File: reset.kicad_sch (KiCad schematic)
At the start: 21 parts, among them J4 MAINCLK

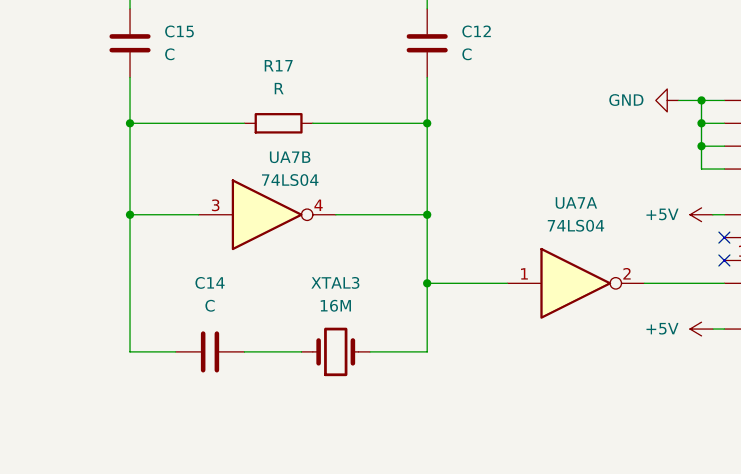
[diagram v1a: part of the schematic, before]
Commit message: Annotated all components
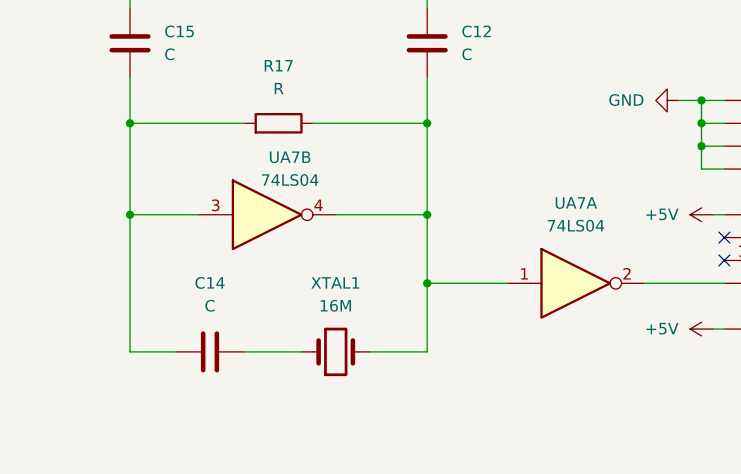
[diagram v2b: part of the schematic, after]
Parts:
- renumbered XTAL3 to XTAL1
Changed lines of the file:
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@@
 		(dnp no)
 		(fields_autoplaced yes)
-		(property "Reference" "XTAL3"
+		(property "Reference" "XTAL1"
 			(at 43.18 177.8 0)
 			(effects
@@
 			(project "ceda"
 				(path "/12a6dbe3-008d-4c5b-88f6-9f1c816060be/d9e42cc5-3ed8-41e5-aab1-e3ef5c13a809"
-					(reference "XTAL3")
+					(reference "XTAL1")
 					(unit 1)
 				)

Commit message: Assigned default footprints to ICs
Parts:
- UA6, UH16: footprint (none) -> Package_DIP:DIP-16_W7.62mm
- UA7, UD14, UD3, UF16, UH15, UL7: footprint (none) -> Package_DIP:DIP-14_W7.62mm
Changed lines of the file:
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@@
 			)
 		)
-		(property "Footprint" ""
+		(property "Footprint" "Package_DIP:DIP-14_W7.62mm"
 			(at 137.16 97.79 0)
 			(effects
@@
 			)
 		)
-		(property "Footprint" ""
+		(property "Footprint" "Package_DIP:DIP-16_W7.62mm"
 			(at 99.06 170.18 0)
 			(effects
@@
 			)
 		)
-		(property "Footprint" ""
+		(property "Footprint" "Package_DIP:DIP-14_W7.62mm"
 			(at 53.34 45.72 0)
 			(effects
@@
 			)
 		)
-		(property "Footprint" ""
+		(property "Footprint" "Package_DIP:DIP-14_W7.62mm"
 			(at 146.05 161.29 0)
 			(effects
@@
 			)
 		)
-		(property "Footprint" ""
+		(property "Footprint" "Package_DIP:DIP-14_W7.62mm"
 			(at 222.25 87.63 0)
 			(effects
@@
 			)
 		)
-		(property "Footprint" ""
+		(property "Footprint" "Package_DIP:DIP-14_W7.62mm"
 			(at 185.42 72.39 0)
 			(effects
@@
 			)
 		)
-		(property "Footprint" ""
+		(property "Footprint" "Package_DIP:DIP-14_W7.62mm"
 			(at 204.47 72.39 0)
 			(effects
@@
 			)
 		)
-		(property "Footprint" ""
+		(property "Footprint" "Package_DIP:DIP-16_W7.62mm"
 			(at 132.08 59.69 0)
 			(effects
@@
 			)
 		)
-		(property "Footprint" ""
+		(property "Footprint" "Package_DIP:DIP-14_W7.62mm"
 			(at 66.04 72.39 0)
 			(effects
@@
 			)
 		)
-		(property "Footprint" ""
+		(property "Footprint" "Package_DIP:DIP-14_W7.62mm"
 			(at 146.05 181.61 0)
 			(effects
@@
 			)
 		)
-		(property "Footprint" ""
+		(property "Footprint" "Package_DIP:DIP-14_W7.62mm"
 			(at 35.56 170.18 0)
 			(effects
@@
 			)
 		)
-		(property "Footprint" ""
+		(property "Footprint" "Package_DIP:DIP-14_W7.62mm"
 			(at 146.05 171.45 0)
 			(effects
@@
 			)
 		)
-		(property "Footprint" ""
+		(property "Footprint" "Package_DIP:DIP-14_W7.62mm"
 			(at 69.85 177.8 0)
 			(effects
@@
 			)
 		)
-		(property "Footprint" ""
+		(property "Footprint" "Package_DIP:DIP-14_W7.62mm"
 			(at 86.36 59.69 0)
 			(effects

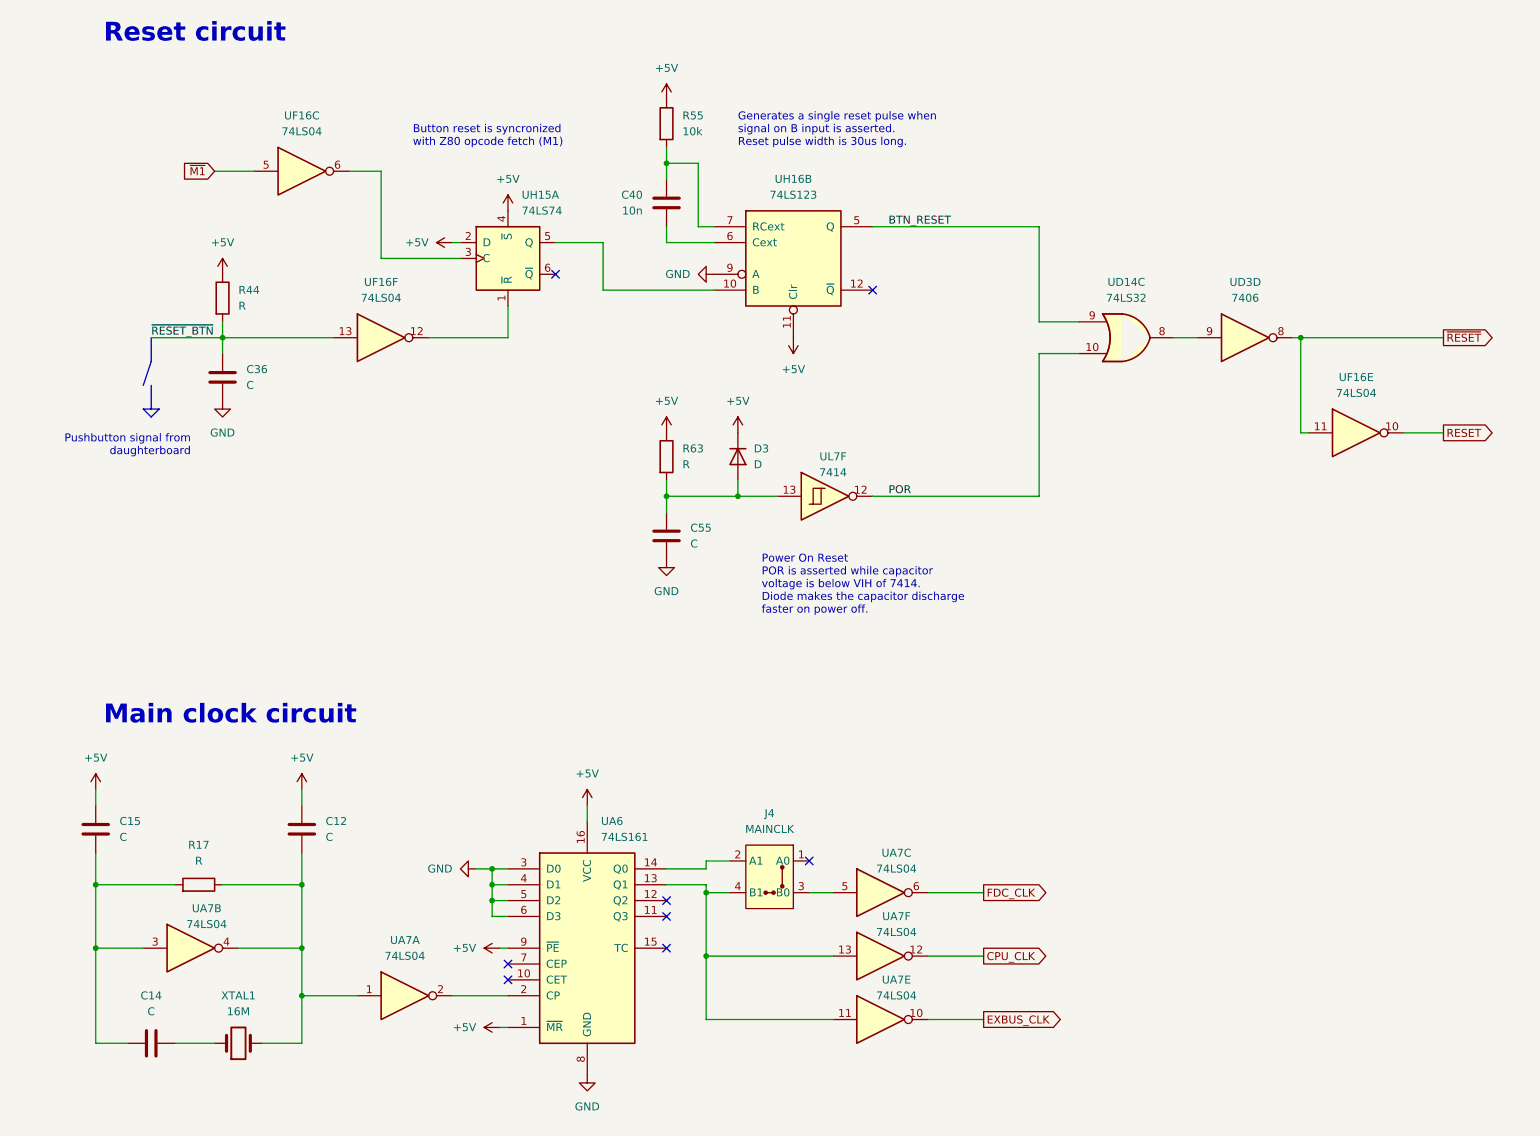
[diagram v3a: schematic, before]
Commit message: pcb: added and placed almost all components
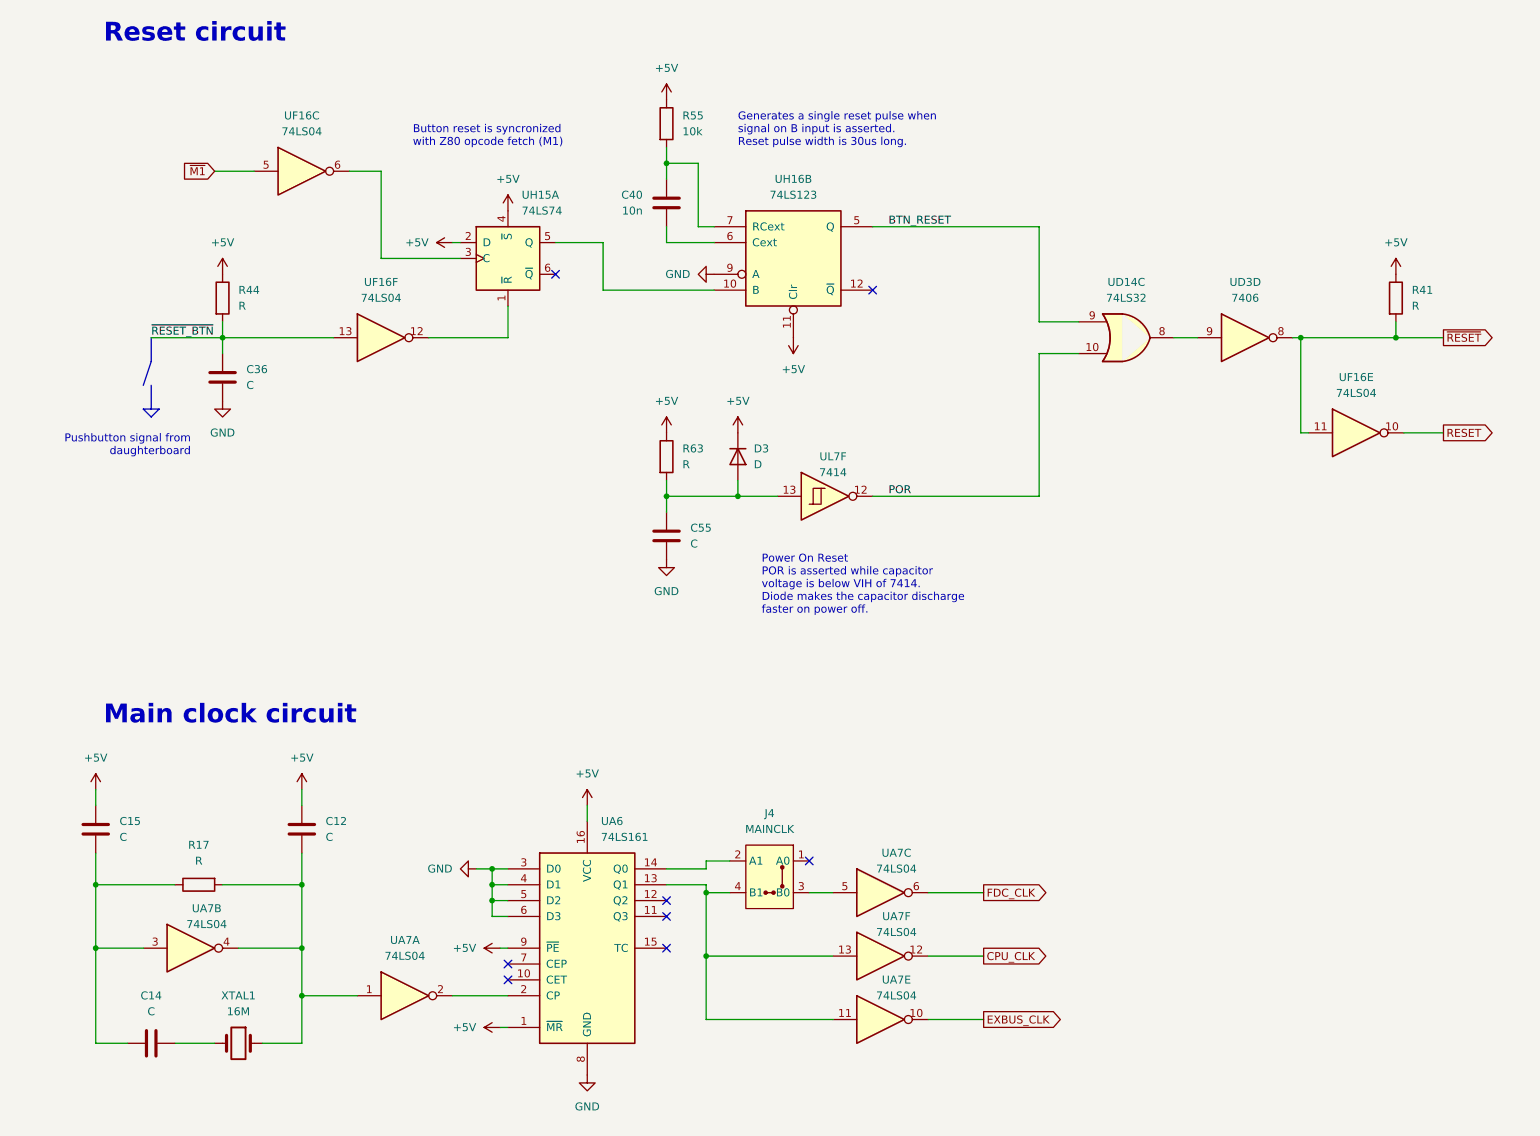
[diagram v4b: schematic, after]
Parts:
- added R41: R, Resistor_THT:R_Axial_DIN0204_L3.6mm_D1.6mm_P5.08mm_Vertical, symbol Device:R
- C12, C14, C15, C36, C40, C55: footprint (none) -> Capacitor_THT:C_Disc_D4.3mm_W1.9mm_P5.00mm
- D3: footprint (none) -> Diode_THT:D_A-405_P5.08mm_Vertical_KathodeUp
- J4: footprint (none) -> Connector_PinHeader_2.54mm:PinHeader_2x02_P2.54mm_Vertical
- R17, R44, R63: footprint (none) -> Resistor_THT:R_Axial_DIN0204_L3.6mm_D1.6mm_P5.08mm_Vertical
- R55: footprint (none) -> Resistor_THT:R_Axial_DIN0309_L9.0mm_D3.2mm_P12.70mm_Horizontal
- XTAL1: footprint (none) -> Crystal:Crystal_HC18-U_Vertical
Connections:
- net +5V: now also R41.1
- net ~{RESET}: now also R41.2
- net at C14.2, C15.1, UA7.3: now also R17.1; no longer R17.2
- net at C14.1: now also XTAL1.2; no longer XTAL1.1
- net at C12.1, UA7.1, UA7.4: now also R17.2, XTAL1.1; no longer R17.1, XTAL1.2
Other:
- moved on the sheet: R17
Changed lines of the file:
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@@
 	)
 	(junction
+		(at 228.6 72.39)
+		(diameter 0)
+		(color 0 0 0 0)
+	)
+	(junction
 		(at 20.32 160.02)
 		(diameter 0)
@@
 	(wire
 		(pts
-			(xy 213.36 72.39) (xy 236.22 72.39)
+			(xy 213.36 72.39) (xy 228.6 72.39)
 		)
 		(stroke
@@
 	(wire
 		(pts
+			(xy 228.6 69.85) (xy 228.6 72.39)
+		)
+		(stroke
+			(width 0)
+			(type default)
+		)
+	)
+	(wire
+		(pts
 			(xy 78.74 57.15) (xy 77.47 57.15)
 		)
@@
 	(wire
 		(pts
+			(xy 228.6 72.39) (xy 236.22 72.39)
+		)
+		(stroke
+			(width 0)
+			(type default)
+		)
+	)
+	(wire
+		(pts
 			(xy 85.09 170.18) (xy 86.36 170.18)
 		)
@@
 	)
 	(symbol
+		(lib_id "Device:R")
+		(at 228.6 66.04 0)
+		(unit 1)
+		(exclude_from_sim no)
+		(in_bom yes)
+		(on_board yes)
+		(dnp no)
+		(fields_autoplaced yes)
+		(property "Reference" "R41"
+			(at 231.14 64.7699 0)
+			(effects
+				(font
+					(size 1.27 1.27)
+				)
+				(justify left)
+			)
+		)
+		(property "Value" "R"
+			(at 231.14 67.3099 0)
+			(effects
+				(font
+					(size 1.27 1.27)
+				)
+				(justify left)
+			)
+		)
+		(property "Footprint" "Resistor_THT:R_Axial_DIN0204_L3.6mm_D1.6mm_P5.08mm_Vertical"
+			(at 226.822 66.04 90)
+			(effects
+				(font
+					(size 1.27 1.27)
+				)
+				(hide yes)
+			)
+		)
+		(property "Datasheet" "~"
+			(at 228.6 66.04 0)
+			(effects
+				(font
+					(size 1.27 1.27)
+				)
+				(hide yes)
+			)
+		)
+		(property "Description" ""
+			(at 228.6 66.04 0)
+			(effects
+				(font
+					(size 1.27 1.27)
+				)
+			)
+		)
+		(pin "1"
+		)
+		(pin "2"
+		)
+		(instances
+			(project "ceda"
+				(path "/12a6dbe3-008d-4c5b-88f6-9f1c816060be/d9e42cc5-3ed8-41e5-aab1-e3ef5c13a809"
+					(reference "R41")
+					(unit 1)
+				)
+			)
+		)
+	)
+	(symbol
 		(lib_id "74xx:74LS14")
 		(at 137.16 97.79 0)
@@
 			)
 		)
-		(property "Footprint" ""
+		(property "Footprint" "Capacitor_THT:C_Disc_D4.3mm_W1.9mm_P5.00mm"
 			(at 19.3548 147.32 0)
 			(effects
@@
 	)
 	(symbol
+		(lib_id "power:+5V")
+		(at 228.6 62.23 0)
+		(unit 1)
+		(exclude_from_sim no)
+		(in_bom yes)
+		(on_board yes)
+		(dnp no)
+		(fields_autoplaced yes)
+		(property "Reference" "#PWR03"
+			(at 228.6 66.04 0)
+			(effects
+				(font
+					(size 1.27 1.27)
+				)
+				(hide yes)
+			)
+		)
+		(property "Value" "+5V"
+			(at 228.6 57.15 0)
+			(effects
+				(font
+					(size 1.27 1.27)
+				)
+			)
+		)
+		(property "Footprint" ""
+			(at 228.6 62.23 0)
+			(effects
+				(font
+					(size 1.27 1.27)
+				)
+				(hide yes)
+			)
+		)
+		(property "Datasheet" ""
+			(at 228.6 62.23 0)
+			(effects
+				(font
+					(size 1.27 1.27)
+				)
+				(hide yes)
+			)
+		)
+		(property "Description" ""
+			(at 228.6 62.23 0)
+			(effects
+				(font
+					(size 1.27 1.27)
+				)
+			)
+		)
+		(pin "1"
+		)
+		(instances
+			(project "ceda"
+				(path "/12a6dbe3-008d-4c5b-88f6-9f1c816060be/d9e42cc5-3ed8-41e5-aab1-e3ef5c13a809"
+					(reference "#PWR03")
+					(unit 1)
+				)
+			)
+		)
+	)
+	(symbol
 		(lib_id "74xx:74LS04")
 		(at 222.25 87.63 0)
@@
 			)
 		)
-		(property "Footprint" ""
+		(property "Footprint" "Resistor_THT:R_Axial_DIN0204_L3.6mm_D1.6mm_P5.08mm_Vertical"
 			(at 109.982 91.44 90)
 			(effects
@@
 			)
 		)
-		(property "Footprint" ""
+		(property "Footprint" "Capacitor_THT:C_Disc_D4.3mm_W1.9mm_P5.00mm"
 			(at 25.4 184.4548 0)
 			(effects
@@
 			)
 		)
-		(property "Footprint" ""
+		(property "Footprint" "Diode_THT:D_A-405_P5.08mm_Vertical_KathodeUp"
 			(at 123.19 91.44 0)
 			(effects
@@
 			)
 		)
-		(property "Footprint" ""
+		(property "Footprint" "Capacitor_THT:C_Disc_D4.3mm_W1.9mm_P5.00mm"
 			(at 112.7252 54.61 0)
 			(effects
@@
 			)
 		)
-		(property "Footprint" ""
+		(property "Footprint" "Capacitor_THT:C_Disc_D4.3mm_W1.9mm_P5.00mm"
 			(at 112.7252 107.95 0)
 			(effects
@@
 			)
 		)
-		(property "Footprint" ""
+		(property "Footprint" "Resistor_THT:R_Axial_DIN0309_L9.0mm_D3.2mm_P12.70mm_Horizontal"
 			(at 109.982 38.1 90)
 			(effects
@@
 			)
 		)
-		(property "Footprint" ""
+		(property "Footprint" "Capacitor_THT:C_Disc_D4.3mm_W1.9mm_P5.00mm"
 			(at 52.3748 147.32 0)
 			(effects
@@
 	(symbol
 		(lib_id "Device:R")
-		(at 36.83 160.02 270)
+		(at 36.83 160.02 90)
 		(mirror x)
 		(unit 1)
@@
 			)
 		)
-		(property "Footprint" ""
-			(at 36.83 161.798 90)
+		(property "Footprint" "Resistor_THT:R_Axial_DIN0204_L3.6mm_D1.6mm_P5.08mm_Vertical"
+			(at 36.83 158.242 90)
 			(effects
 				(font
@@
 			)
 		)
-		(property "Footprint" ""
+		(property "Footprint" "Connector_PinHeader_2.54mm:PinHeader_2x02_P2.54mm_Vertical"
 			(at 128.27 161.29 0)
 			(effects
@@
 			)
 		)
-		(property "Footprint" ""
+		(property "Footprint" "Capacitor_THT:C_Disc_D4.3mm_W1.9mm_P5.00mm"
 			(at 41.6052 82.55 0)
 			(effects
@@
 		(lib_id "Device:Crystal")
 		(at 43.18 185.42 0)
-		(mirror x)
+		(mirror y)
 		(unit 1)
 		(exclude_from_sim no)
@@
 			)
 		)
-		(property "Footprint" ""
+		(property "Footprint" "Crystal:Crystal_HC18-U_Vertical"
 			(at 43.18 185.42 0)
 			(effects
@@
 			)
 		)
-		(property "Footprint" ""
+		(property "Footprint" "Resistor_THT:R_Axial_DIN0204_L3.6mm_D1.6mm_P5.08mm_Vertical"
 			(at 38.862 66.04 90)
 			(effects
